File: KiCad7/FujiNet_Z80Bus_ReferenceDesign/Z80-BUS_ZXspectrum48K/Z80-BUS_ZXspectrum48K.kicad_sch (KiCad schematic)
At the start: 5 parts, among them J1 DIAG-HOST_SYSTEM_BUS, J2 HOST SYSTEM HEADER

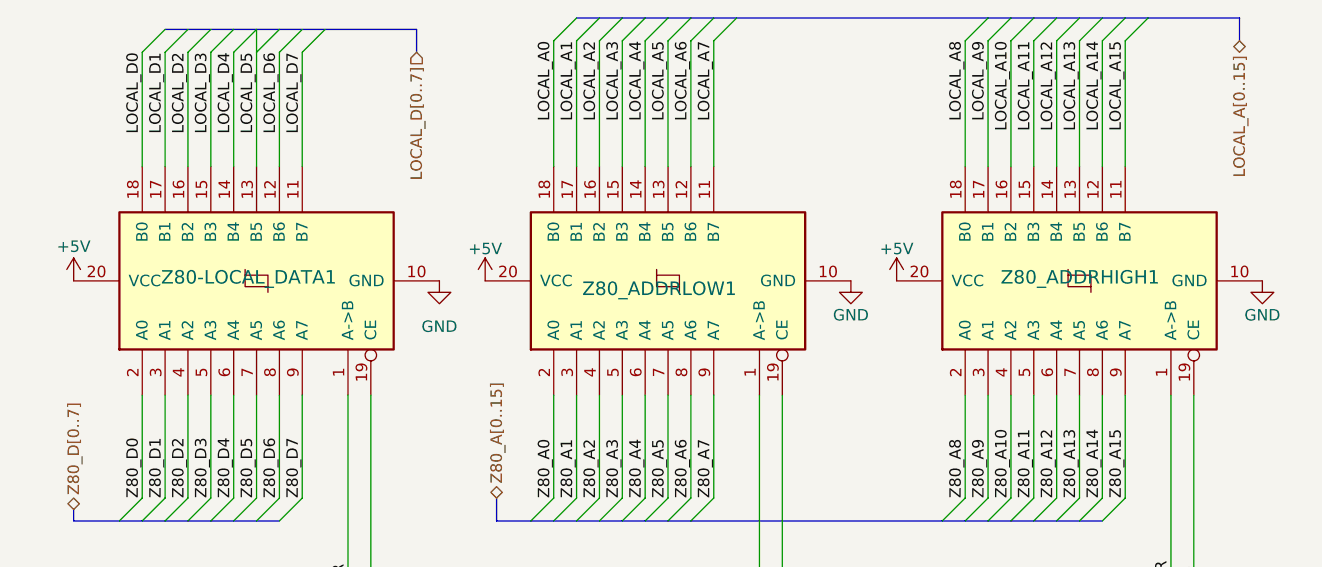
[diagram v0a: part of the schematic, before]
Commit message: KiCad - Refactor Z80_BUS to Z80-BUS_ZXspectrum48K
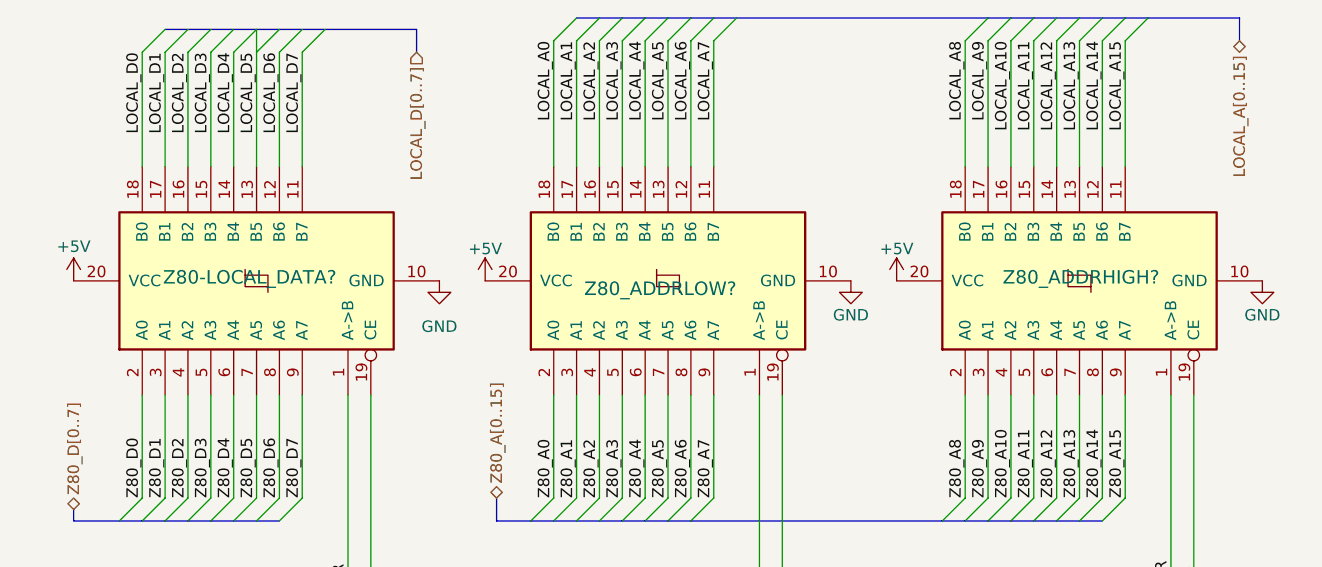
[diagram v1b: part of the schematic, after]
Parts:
- renumbered Z80-LOCAL_DATA1 to Z80-LOCAL_DATA?, Z80_ADDRHIGH1 to Z80_ADDRHIGH?, Z80_ADDRLOW1 to Z80_ADDRLOW?
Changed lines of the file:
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@@
   (symbol (lib_id "74xx:74HC245") (at 57.15 45.72 90) (unit 1)
     (in_bom yes) (on_board yes) (dnp no)
-    (property "Reference" "Z80-LOCAL_DATA1" (at 66.04 44.45 90)
+    (property "Reference" "Z80-LOCAL_DATA?" (at 66.04 44.45 90)
       (effects (font (size 1.4986 1.4986)) (justify left bottom))
     )
@@
     (instances
       (project "FujiNet_Z80Bus_ReferenceDesign"
+        (path "/532c0392-800e-45cc-8170-6d32f2390e83"
+          (reference "Z80-LOCAL_DATA?") (unit 1)
+        )
         (path "/532c0392-800e-45cc-8170-6d32f2390e83/00000000-0000-0000-0000-0000ade3baf4"
           (reference "Z80-LOCAL_DATA1") (unit 1)
-        )
-        (path "/532c0392-800e-45cc-8170-6d32f2390e83"
-          (reference "Z80-LOCAL_DATA?") (unit 1)
         )
       )
@@
   (symbol (lib_id "74xx:74HC245") (at 148.59 45.72 90) (unit 1)
     (in_bom yes) (on_board yes) (dnp no)
-    (property "Reference" "Z80_ADDRHIGH1" (at 157.48 44.45 90)
+    (property "Reference" "Z80_ADDRHIGH?" (at 157.48 44.45 90)
       (effects (font (size 1.4986 1.4986)) (justify left bottom))
     )
@@
     (instances
       (project "FujiNet_Z80Bus_ReferenceDesign"
+        (path "/532c0392-800e-45cc-8170-6d32f2390e83"
+          (reference "Z80_ADDRHIGH?") (unit 1)
+        )
         (path "/532c0392-800e-45cc-8170-6d32f2390e83/00000000-0000-0000-0000-0000ade3baf4"
           (reference "Z80_ADDRHIGH1") (unit 1)
-        )
-        (path "/532c0392-800e-45cc-8170-6d32f2390e83"
-          (reference "Z80_ADDRHIGH?") (unit 1)
         )
       )
@@
   (symbol (lib_id "74xx:74HC245") (at 102.87 45.72 90) (unit 1)
     (in_bom yes) (on_board yes) (dnp no)
-    (property "Reference" "Z80_ADDRLOW1" (at 110.49 45.72 90)
+    (property "Reference" "Z80_ADDRLOW?" (at 110.49 45.72 90)
       (effects (font (size 1.4986 1.4986)) (justify left bottom))
     )
@@
     (instances
       (project "FujiNet_Z80Bus_ReferenceDesign"
+        (path "/532c0392-800e-45cc-8170-6d32f2390e83"
+          (reference "Z80_ADDRLOW?") (unit 1)
+        )
         (path "/532c0392-800e-45cc-8170-6d32f2390e83/00000000-0000-0000-0000-0000ade3baf4"
           (reference "Z80_ADDRLOW1") (unit 1)
         )
-        (path "/532c0392-800e-45cc-8170-6d32f2390e83"
-          (reference "Z80_ADDRLOW?") (unit 1)
-        )
       )

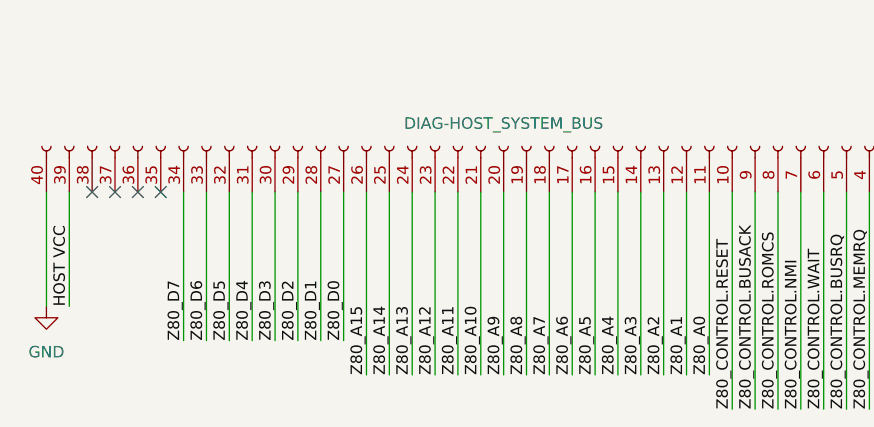
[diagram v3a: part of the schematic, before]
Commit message: KiCad - Proof of concept PCB in-progress
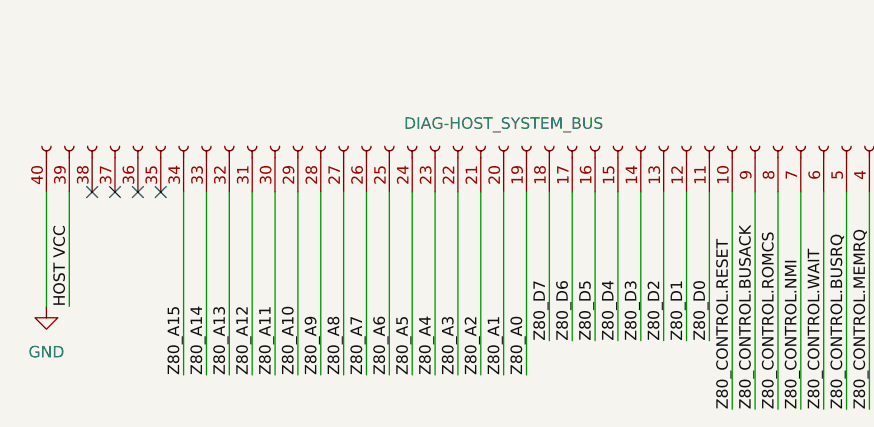
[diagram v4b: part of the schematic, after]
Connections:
- net Z80_A0: now also J1.19 (Pin_19); no longer J1.11 (Pin_11)
- net Z80_A1: now also J1.20 (Pin_20); no longer J1.12 (Pin_12)
- net Z80_A10: now also J1.29 (Pin_29); no longer J1.21 (Pin_21)
- net Z80_A11: now also J1.30 (Pin_30); no longer J1.22 (Pin_22)
- net Z80_A12: now also J1.31 (Pin_31); no longer J1.23 (Pin_23)
- net Z80_A13: now also J1.32 (Pin_32); no longer J1.24 (Pin_24)
- net Z80_A14: now also J1.33 (Pin_33); no longer J1.25 (Pin_25)
- net Z80_A15: now also J1.34 (Pin_34); no longer J1.26 (Pin_26)
- net Z80_A2: now also J1.21 (Pin_21); no longer J1.13 (Pin_13)
- net Z80_A3: now also J1.22 (Pin_22); no longer J1.14 (Pin_14)
- net Z80_A4: now also J1.23 (Pin_23); no longer J1.15 (Pin_15)
- net Z80_A5: now also J1.24 (Pin_24); no longer J1.16 (Pin_16)
- net Z80_A6: now also J1.25 (Pin_25); no longer J1.17 (Pin_17)
- net Z80_A7: now also J1.26 (Pin_26); no longer J1.18 (Pin_18)
- net Z80_A8: now also J1.27 (Pin_27); no longer J1.19 (Pin_19)
- net Z80_A9: now also J1.28 (Pin_28); no longer J1.20 (Pin_20)
- net Z80_D0: now also J1.11 (Pin_11); no longer J1.27 (Pin_27)
- net Z80_D1: now also J1.12 (Pin_12); no longer J1.28 (Pin_28)
- net Z80_D2: now also J1.13 (Pin_13); no longer J1.29 (Pin_29)
- net Z80_D3: now also J1.14 (Pin_14); no longer J1.30 (Pin_30)
- net Z80_D4: now also J1.15 (Pin_15); no longer J1.31 (Pin_31)
- net Z80_D5: now also J1.16 (Pin_16); no longer J1.32 (Pin_32)
- net Z80_D6: now also J1.17 (Pin_17); no longer J1.33 (Pin_33)
- net Z80_D7: now also J1.18 (Pin_18); no longer J1.34 (Pin_34)

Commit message: KiCad Prototype routing (failed)
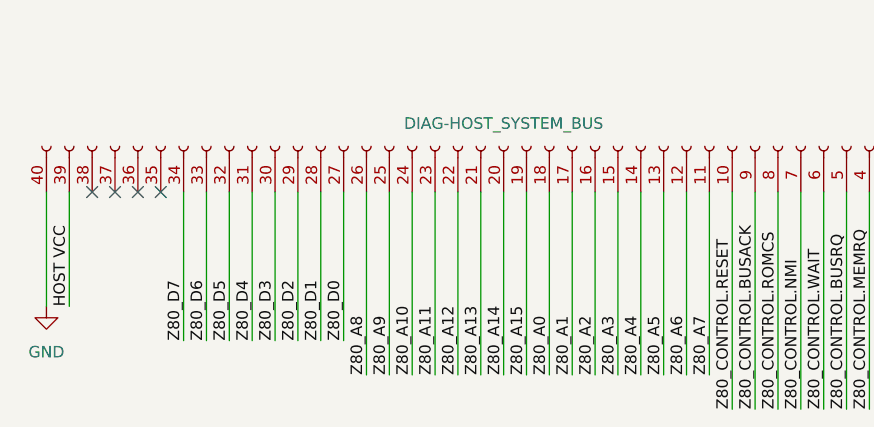
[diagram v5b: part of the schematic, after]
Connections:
- net Z80_A0: now also J1.18 (Pin_18); no longer J1.19 (Pin_19)
- net Z80_A1: now also J1.17 (Pin_17); no longer J1.20 (Pin_20)
- net Z80_A10: now also J1.24 (Pin_24); no longer J1.29 (Pin_29)
- net Z80_A11: now also J1.23 (Pin_23); no longer J1.30 (Pin_30)
- net Z80_A12: now also J1.22 (Pin_22); no longer J1.31 (Pin_31)
- net Z80_A13: now also J1.21 (Pin_21); no longer J1.32 (Pin_32)
- net Z80_A14: now also J1.20 (Pin_20); no longer J1.33 (Pin_33)
- net Z80_A15: now also J1.19 (Pin_19); no longer J1.34 (Pin_34)
- net Z80_A2: now also J1.16 (Pin_16); no longer J1.21 (Pin_21)
- net Z80_A3: now also J1.15 (Pin_15); no longer J1.22 (Pin_22)
- net Z80_A4: now also J1.14 (Pin_14); no longer J1.23 (Pin_23)
- net Z80_A5: now also J1.13 (Pin_13); no longer J1.24 (Pin_24)
- net Z80_A6: now also J1.12 (Pin_12); no longer J1.25 (Pin_25)
- net Z80_A7: now also J1.11 (Pin_11); no longer J1.26 (Pin_26)
- net Z80_A8: now also J1.26 (Pin_26); no longer J1.27 (Pin_27)
- net Z80_A9: now also J1.25 (Pin_25); no longer J1.28 (Pin_28)
- net Z80_D0: now also J1.27 (Pin_27); no longer J1.11 (Pin_11)
- net Z80_D1: now also J1.28 (Pin_28); no longer J1.12 (Pin_12)
- net Z80_D2: now also J1.29 (Pin_29); no longer J1.13 (Pin_13)
- net Z80_D3: now also J1.30 (Pin_30); no longer J1.14 (Pin_14)
- net Z80_D4: now also J1.31 (Pin_31); no longer J1.15 (Pin_15)
- net Z80_D5: now also J1.32 (Pin_32); no longer J1.16 (Pin_16)
- net Z80_D6: now also J1.33 (Pin_33); no longer J1.17 (Pin_17)
- net Z80_D7: now also J1.34 (Pin_34); no longer J1.18 (Pin_18)

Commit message: KiCad - First prototype routed
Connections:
- net Z80_D0: now also J1.34 (Pin_34); no longer J1.27 (Pin_27)
- net Z80_D1: now also J1.33 (Pin_33); no longer J1.28 (Pin_28)
- net Z80_D2: now also J1.32 (Pin_32); no longer J1.29 (Pin_29)
- net Z80_D3: now also J1.31 (Pin_31); no longer J1.30 (Pin_30)
- net Z80_D4: now also J1.30 (Pin_30); no longer J1.31 (Pin_31)
- net Z80_D5: now also J1.29 (Pin_29); no longer J1.32 (Pin_32)
- net Z80_D6: now also J1.28 (Pin_28); no longer J1.33 (Pin_33)
- net Z80_D7: now also J1.27 (Pin_27); no longer J1.34 (Pin_34)
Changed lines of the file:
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@@
     (effects (font (size 1.27 1.27)) (justify right bottom))
   )
-  (label "Z80_D0" (at 82.55 168.91 90) (fields_autoplaced)
+  (label "Z80_D0" (at 64.77 168.91 90) (fields_autoplaced)
     (effects (font (size 1.27 1.27)) (justify left bottom))
   )
@@
     (effects (font (size 1.27 1.27)) (justify left bottom))
   )
-  (label "Z80_D2" (at 77.47 168.91 90) (fields_autoplaced)
+  (label "Z80_D2" (at 69.85 168.91 90) (fields_autoplaced)
     (effects (font (size 1.27 1.27)) (justify left bottom))
   )
@@
     (effects (font (size 1.27 1.27)) (justify right bottom))
   )
-  (label "Z80_D5" (at 69.85 168.91 90) (fields_autoplaced)
-    (effects (font (size 1.27 1.27)) (justify left bottom))
-  )
-  (label "Z80_D6" (at 67.31 168.91 90) (fields_autoplaced)
+  (label "Z80_D5" (at 77.47 168.91 90) (fields_autoplaced)
+    (effects (font (size 1.27 1.27)) (justify left bottom))
+  )
+  (label "Z80_D6" (at 80.01 168.91 90) (fields_autoplaced)
     (effects (font (size 1.27 1.27)) (justify left bottom))
   )
@@
     (effects (font (size 1.27 1.27)) (justify right bottom))
   )
-  (label "Z80_D4" (at 72.39 168.91 90) (fields_autoplaced)
+  (label "Z80_D4" (at 74.93 168.91 90) (fields_autoplaced)
     (effects (font (size 1.27 1.27)) (justify left bottom))
   )
@@
     (effects (font (size 1.27 1.27)) (justify left bottom))
   )
-  (label "Z80_D3" (at 74.93 168.91 90) (fields_autoplaced)
+  (label "Z80_D3" (at 72.39 168.91 90) (fields_autoplaced)
     (effects (font (size 1.27 1.27)) (justify left bottom))
   )
@@
     (effects (font (size 1.27 1.27)) (justify left bottom))
   )
-  (label "Z80_D7" (at 64.77 168.91 90) (fields_autoplaced)
+  (label "Z80_D7" (at 82.55 168.91 90) (fields_autoplaced)
     (effects (font (size 1.27 1.27)) (justify left bottom))
   )
@@
     (effects (font (size 1.27 1.27)) (justify left bottom))
   )
-  (label "Z80_D1" (at 80.01 168.91 90) (fields_autoplaced)
-    (effects (font (size 1.27 1.27)) (justify left bottom))
-  )
+  (label "Z80_D1" (at 67.31 168.91 90) (fields_autoplaced)
+    (effects (font (size 1.27 1.27)) (justify left bottom))
+  )
